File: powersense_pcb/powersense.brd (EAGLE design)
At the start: 65 x 57.8 mm, 66 parts, among them IC1 ADG608R, IC2 LM741D, U1 LT1494CS8PBF, U2 LT1494CS8PBF, U3 LM77051, U4 BQ25504RGT, U5 SIP32431DR3, X1 1727036, X2 1727036, X3 1727036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

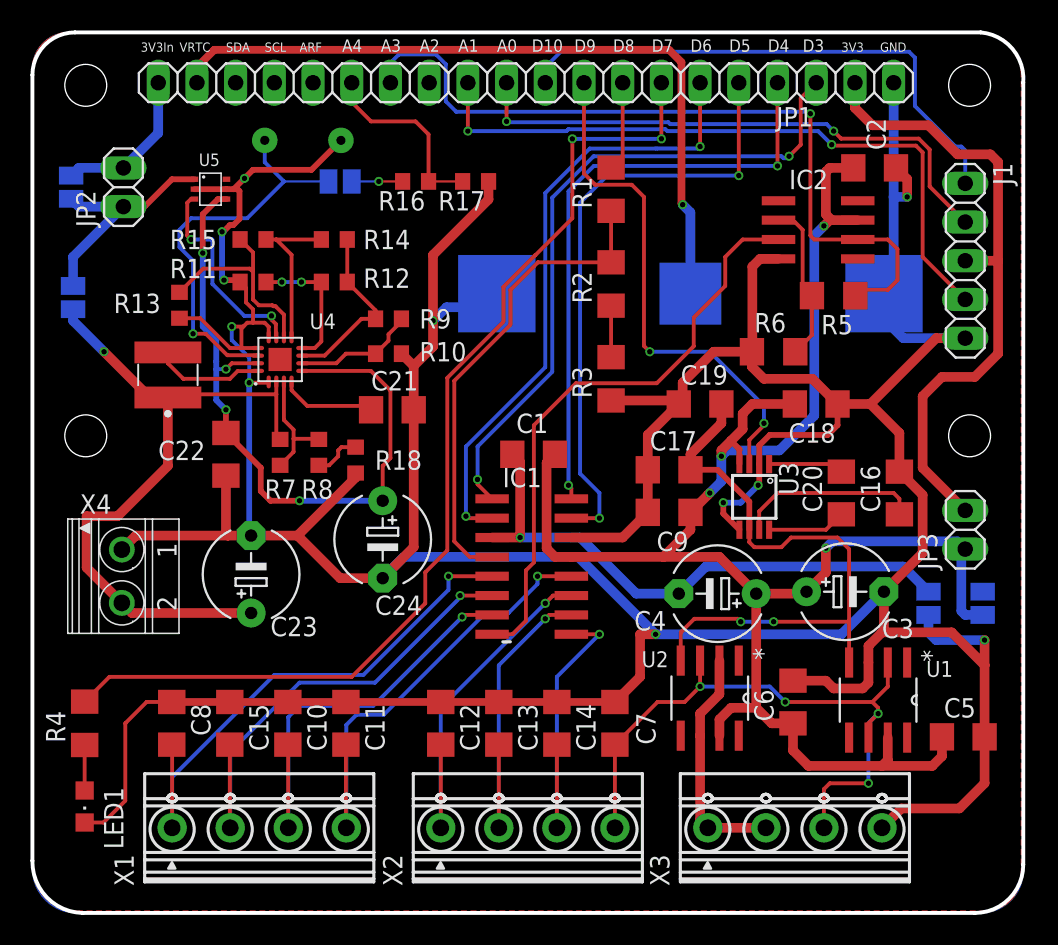
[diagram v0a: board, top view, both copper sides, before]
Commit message: changed coin cell holder
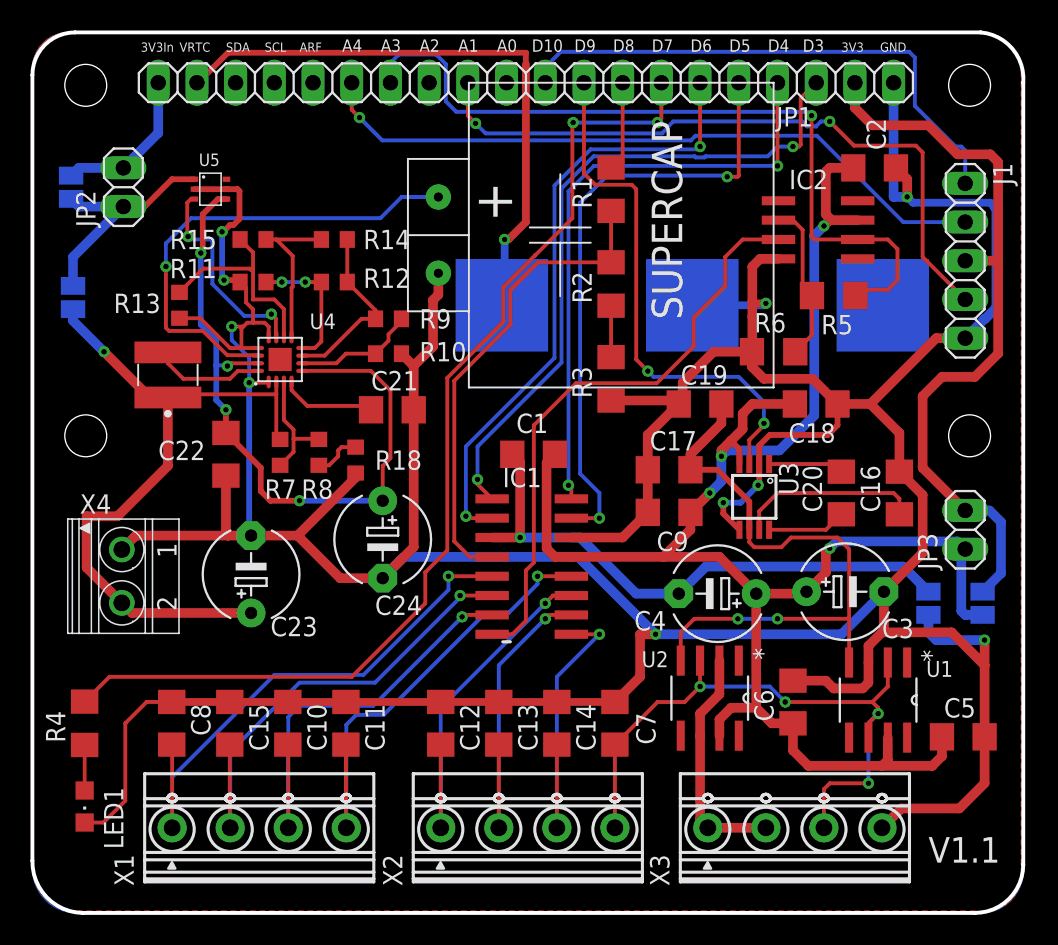
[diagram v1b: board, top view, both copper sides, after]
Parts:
- removed R16: PD1, rcl:R0603
- removed R17: PD2, rcl:R0603
- removed SJ3: (no value), jumper:SJ
- removed U$1: (no value), adafruit:CR2032-SMD
- added BT1: (no value), SparkFun-Batteries:BATTCON_20MM
- moved U$2 48.3 mm to (96.9, 62.2), flipped to the top, turned to 270 degrees
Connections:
- removed net N$11: R16.2, SJ3.2
- net A0: no longer J1.2
- net A4: now also J1.2; no longer R16.1, R17.2
- net GND: now also BT1.2; no longer R17.1, U$1.+$1, U$1.+$2
- net JEFF: no longer SJ3.1
- net VRTC: now also BT1.1; no longer U$1.-
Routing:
- net A0: track 36.8 -> 0.00 mm, vias 2 -> 0
- net A4: track 12.5 -> 45.3 mm, vias 0 -> 1
- net GND: track 342.3 -> 328.4 mm, vias 11 -> 10
- net VRTC: track 49.2 -> 39.8 mm
- net 3V3: track 42.0 -> 49.8 mm
- net JEFF: track 26.3 -> 31.5 mm
- net N$11: track 3.34 -> 0.00 mm, vias 1 -> 0
- net D9: track 34.0 -> 35.0 mm
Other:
- board text added: "V1.1"
